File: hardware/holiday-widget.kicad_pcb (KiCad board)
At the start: 4 copper layers, 150 x 75 mm, 119 parts, among them J2 UART, J33 Conn_02x05_Odd_Even, J4 BATTERY POWER, J5 VDC POWER, J7 Speaker, Q1 MMBT3906, Q2 MMBT3906, Q3 MMBT3906, Q4 MMBT3906, Q5 MMBT3906, Q6 MMBT3906, Q7 MMBT3906, Q8 MMBT3906, SW1 SW_Push, SW4 SW_Push, U1 STM32L072RBTx, U2 TPS61200DRC, U3 LIS3DH, U4 IMP23ABSU, U5 TMP102xxDRL, U6 VCNL_4020, U7 PAM8302AAD, U8 OPA355NA

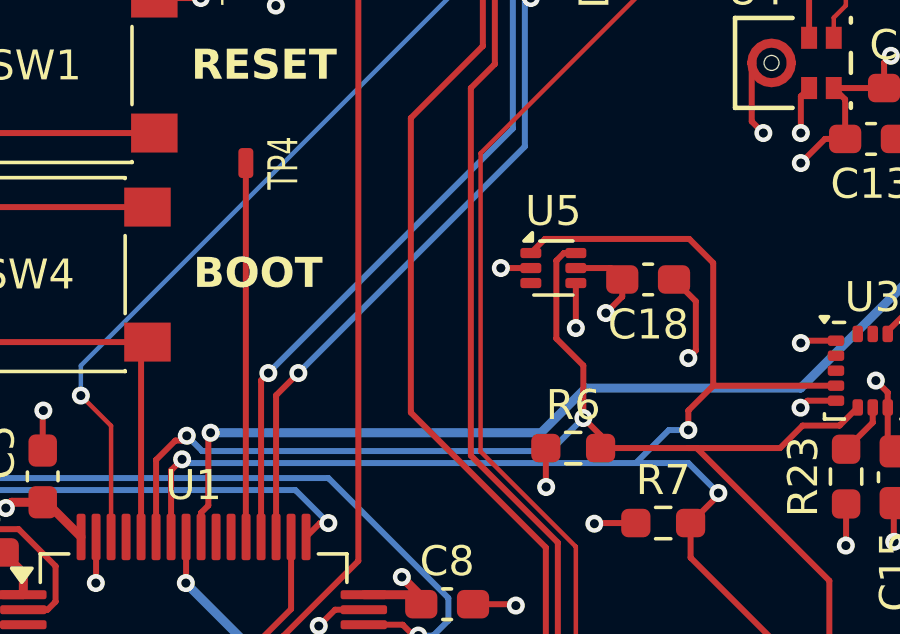
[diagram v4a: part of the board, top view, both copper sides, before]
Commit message: [Hardware] Remove tmp102
No longer using the tmp102 temperature sensor, so remove it from the board.
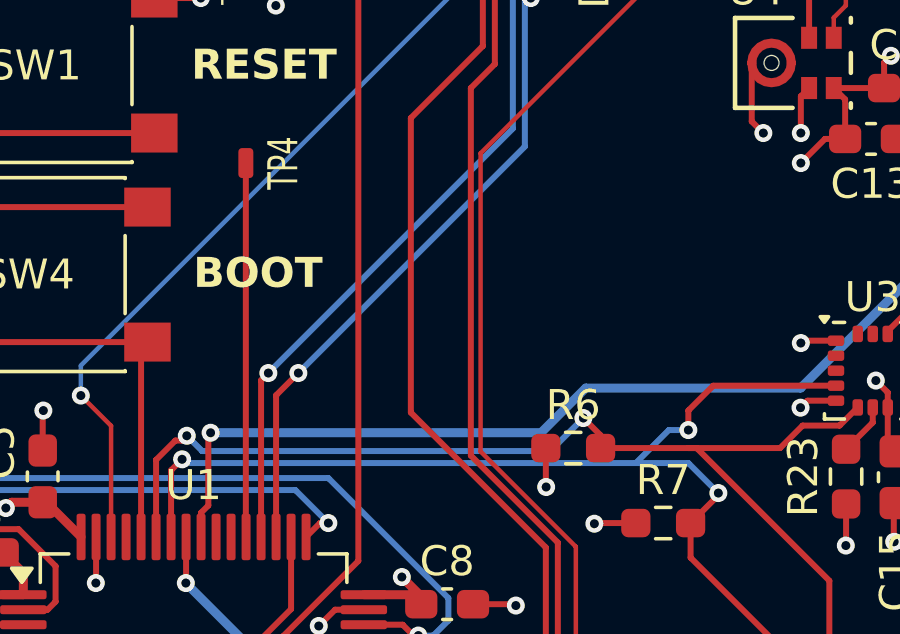
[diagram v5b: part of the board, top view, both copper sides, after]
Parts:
- removed C18: 10n, Capacitor_SMD:C_0603_1608Metric_Pad1.08x0.95mm_HandSolder
- removed U5: TMP102xxDRL, Package_TO_SOT_SMD:SOT-563
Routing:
- net /I2C.SCL: track 111.2 -> 100.5 mm
- net /I2C.SDA: track 103.4 -> 97.0 mm
- net /GND: track 100.0 -> 94.5 mm, vias 63 -> 60
- net /VDD: track 82.2 -> 79.2 mm, vias 32 -> 31

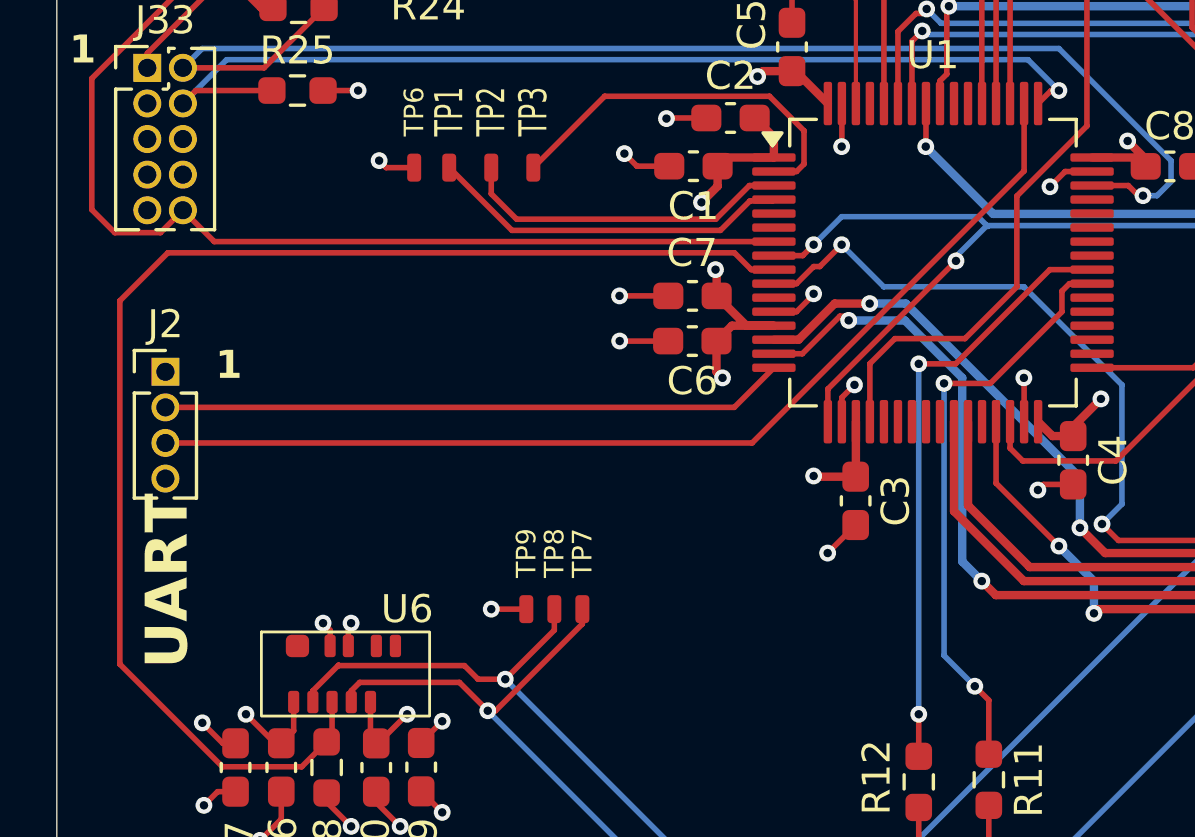
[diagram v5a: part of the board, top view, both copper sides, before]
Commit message: [Hardware] Resize UART header to be 2.54mm pitch.
Previous revision had incorrectly sized pinout, correct this.
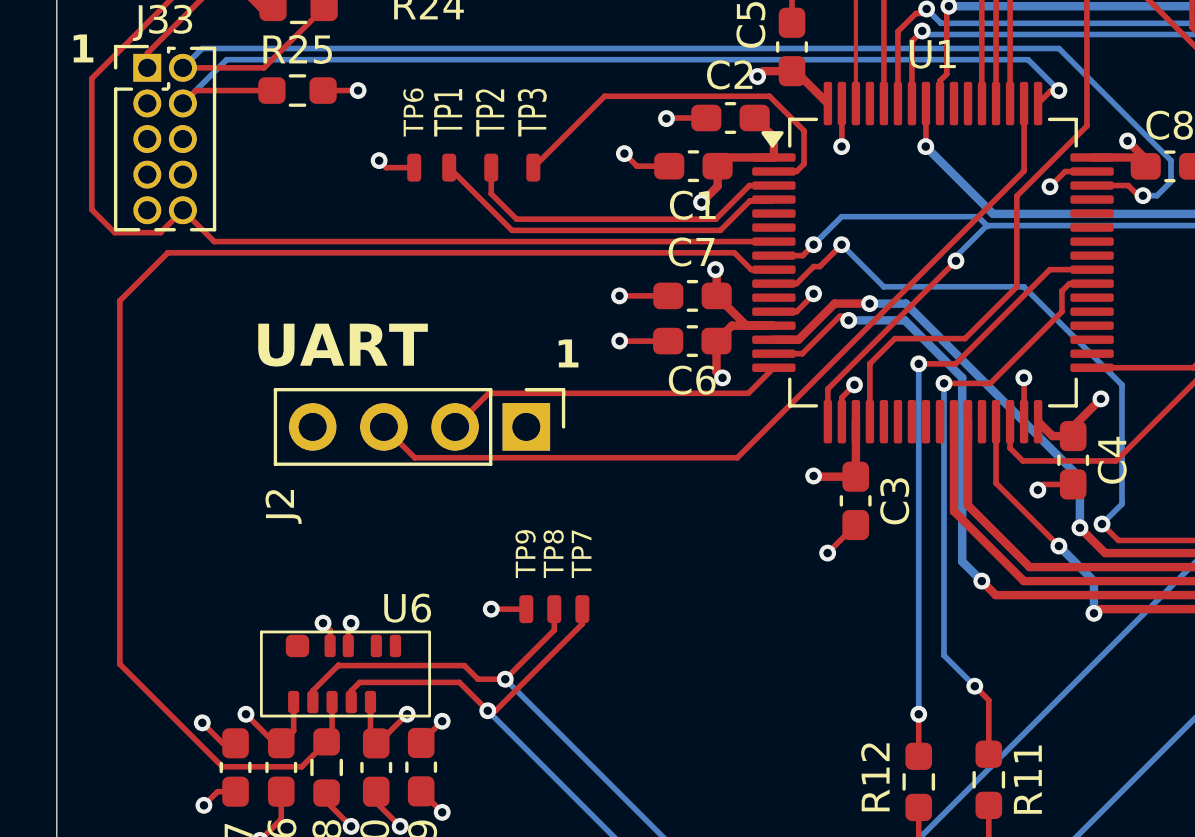
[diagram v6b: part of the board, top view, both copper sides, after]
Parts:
- J2: footprint Connector_PinHeader_1.27mm:PinHeader_1x04_P1.27mm_Vertical -> Connector_PinHeader_2.54mm:PinHeader_1x04_P2.54mm_Vertical
- moved J2 13.0 mm to (130.8, 125.0), turned to -90 degrees
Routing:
- net /UART.TX: track 22.3 -> 12.2 mm
- net /UART.RX: track 37.1 -> 29.9 mm
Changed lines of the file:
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@@
 		)
 	)
-	(footprint "Connector_PinHeader_1.27mm:PinHeader_1x04_P1.27mm_Vertical"
+	(footprint "Connector_PinHeader_2.54mm:PinHeader_1x04_P2.54mm_Vertical"
 		(layer "F.Cu")
-		(at 117.87536 123.032355)
-		(descr "Through hole straight pin header, 1x04, 1.27mm pitch, single row")
-		(tags "Through hole pin header THT 1x04 1.27mm single row")
+		(at 130.75 125 -90)
+		(descr "Through hole straight pin header, 1x04, 2.54mm pitch, single row")
+		(tags "Through hole pin header THT 1x04 2.54mm single row")
 		(property "Reference" "J2"
-			(at 0 -1.695 0)
+			(at 2.75 8.75 90)
 			(layer "F.SilkS")
 			(effects
 				(font
 					(size 1 1)
-					(thickness 0.153)
+					(thickness 0.15)
 				)
 			)
 		)
 		(property "Value" "UART"
-			(at 0 5.505 0)
+			(at 0 9.95 90)
 			(layer "F.Fab")
 			(effects
@@
 			)
 		)
-		(property "Footprint" "Connector_PinHeader_1.27mm:PinHeader_1x04_P1.27mm_Vertical"
-			(at 0 0 0)
+		(property "Footprint" "Connector_PinHeader_2.54mm:PinHeader_1x04_P2.54mm_Vertical"
+			(at 0 0 -90)
 			(unlocked yes)
 			(layer "F.Fab")
@@
 		)
 		(property "Datasheet" ""
-			(at 0 0 0)
+			(at 0 0 -90)
 			(unlocked yes)
 			(layer "F.Fab")
@@
 		)
 		(property "Description" "Generic connector, single row, 01x04, script generated (kicad-library-utils/schlib/autogen/connector/)"
-			(at 0 0 0)
+			(at 0 0 -90)
 			(unlocked yes)
 			(layer "F.Fab")
@@
 		(attr through_hole)
 		(fp_line
-			(start -1.11 -0.76)
-			(end 0 -0.76)
+			(start -1.33 8.95)
+			(end 1.33 8.95)
 			(stroke
 				(width 0.12)
@@
 		)
 		(fp_line
-			(start -1.11 0)
-			(end -1.11 -0.76)
+			(start -1.33 1.27)
+			(end -1.33 8.95)
 			(stroke
 				(width 0.12)
@@
 		)
 		(fp_line
-			(start -1.11 0.76)
-			(end -1.11 4.505)
+			(start -1.33 1.27)
+			(end 1.33 1.27)
 			(stroke
 				(width 0.12)
@@
 		)
 		(fp_line
-			(start -1.11 0.76)
-			(end -0.563471 0.76)
+			(start 1.33 1.27)
+			(end 1.33 8.95)
 			(stroke
 				(width 0.12)
@@
 		)
 		(fp_line
-			(start -1.11 4.505)
-			(end -0.30753 4.505)
+			(start -1.33 0)
+			(end -1.33 -1.33)
 			(stroke
 				(width 0.12)
@@
 		)
 		(fp_line
-			(start 0.30753 4.505)
-			(end 1.11 4.505)
+			(start -1.33 -1.33)
+			(end 0 -1.33)
 			(stroke
 				(width 0.12)
@@
 		)
 		(fp_line
-			(start 0.563471 0.76)
-			(end 1.11 0.76)
-			(stroke
-				(width 0.12)
-				(type solid)
-			)
-			(layer "F.SilkS")
-		)
-		(fp_line
-			(start 1.11 0.76)
-			(end 1.11 4.505)
-			(stroke
-				(width 0.12)
-				(type solid)
-			)
-			(layer "F.SilkS")
-		)
-		(fp_line
-			(start -1.55 -1.15)
-			(end -1.55 4.95)
+			(start -1.8 9.4)
+			(end 1.8 9.4)
 			(stroke
 				(width 0.05)
@@
 		)
 		(fp_line
-			(start -1.55 4.95)
-			(end 1.55 4.95)
+			(start 1.8 9.4)
+			(end 1.8 -1.8)
 			(stroke
 				(width 0.05)
@@
 		)
 		(fp_line
-			(start 1.55 -1.15)
-			(end -1.55 -1.15)
+			(start -1.8 -1.8)
+			(end -1.8 9.4)
 			(stroke
 				(width 0.05)
@@
 		)
 		(fp_line
-			(start 1.55 4.95)
-			(end 1.55 -1.15)
+			(start 1.8 -1.8)
+			(end -1.8 -1.8)
 			(stroke
 				(width 0.05)
@@
 		)
 		(fp_line
-			(start -1.05 -0.11)
-			(end -0.525 -0.635)
+			(start -1.27 8.89)
+			(end -1.27 -0.635)
 			(stroke
 				(width 0.1)
@@
 		)
 		(fp_line
-			(start -1.05 4.445)
-			(end -1.05 -0.11)
+			(start 1.27 8.89)
+			(end -1.27 8.89)
 			(stroke
 				(width 0.1)
@@
 		)
 		(fp_line
-			(start -0.525 -0.635)
-			(end 1.05 -0.635)
+			(start -1.27 -0.635)
+			(end -0.635 -1.27)
 			(stroke
 				(width 0.1)
@@
 		)
 		(fp_line
-			(start 1.05 -0.635)
-			(end 1.05 4.445)
+			(start -0.635 -1.27)
+			(end 1.27 -1.27)
 			(stroke
 				(width 0.1)
@@
 		)
 		(fp_line
-			(start 1.05 4.445)
-			(end -1.05 4.445)
+			(start 1.27 -1.27)
+			(end 1.27 8.89)
 			(stroke
 				(width 0.1)
@@
 		)
 		(fp_text user "${REFERENCE}"
-			(at 0 1.905 90)
+			(at 0 3.81 360)
 			(layer "F.Fab")
 			(effects
@@
 		)
 		(pad "1" thru_hole rect
-			(at 0 0)
-			(size 1 1)
-			(drill 0.65)
+			(at 0 0 270)
+			(size 1.7 1.7)
+			(drill 1)
 			(layers "*.Cu" "*.Mask")
 			(remove_unused_layers no)
@@
 		)
 		(pad "2" thru_hole oval
-			(at 0 1.27)
-			(size 1 1)
-			(drill 0.65)
+			(at 0 2.54 270)
+			(size 1.7 1.7)
+			(drill 1)
 			(layers "*.Cu" "*.Mask")
 			(remove_unused_layers no)
@@
 		)
 		(pad "3" thru_hole oval
-			(at 0 2.54)
-			(size 1 1)
-			(drill 0.65)
+			(at 0 5.08 270)
+			(size 1.7 1.7)
+			(drill 1)
 			(layers "*.Cu" "*.Mask")
 			(remove_unused_layers no)
@@
 		)
 		(pad "4" thru_hole oval
-			(at 0 3.81)
-			(size 1 1)
-			(drill 0.65)
+			(at 0 7.62 270)
+			(size 1.7 1.7)
+			(drill 1)
 			(layers "*.Cu" "*.Mask")
 			(remove_unused_layers no)
@@
 			(pintype "passive")
 		)
-		(model "${KICAD8_3DMODEL_DIR}/Connector_PinHeader_1.27mm.3dshapes/PinHeader_1x04_P1.27mm_Vertical.wrl"
+		(model "${KICAD8_3DMODEL_DIR}/Connector_PinHeader_2.54mm.3dshapes/PinHeader_1x04_P2.54mm_Vertical.wrl"
 			(offset
 				(xyz 0 0 0)
@@
 	)
 	(gr_text "UART"
-		(at 118.818028 133.620197 90)
+		(at 121 123 0)
 		(layer "F.SilkS")
 		(effects
@@
 	)
 	(gr_text "1"
-		(at 119.66126 123.371122 0)
+		(at 131.75 123 0)
 		(layer "F.SilkS")
 		(effects
@@
 	)
 	(segment
-		(start 138.169305 124.302355)
-		(end 139.582934 122.888726)
+		(start 138.67166 123.8)
+		(end 129.41 123.8)
 		(width 0.2)
 		(layer "F.Cu")
@@
 	)
 	(segment
-		(start 117.87536 124.302355)
-		(end 138.169305 124.302355)
+		(start 139.582934 122.888726)
+		(end 138.67166 123.8)
 		(width 0.2)
 		(layer "F.Cu")
@@
 	)
 	(segment
-		(start 148.507934 113.463726)
-		(end 148.507934 115.869884)
+		(start 129.41 123.8)
+		(end 128.21 125)
+		(width 0.2)
+		(layer "F.Cu")
+		(net 12)
+	)
+	(segment
+		(start 148.507934 115.869884)
+		(end 138.277818 126.1)
 		(width 0.2)
 		(layer "F.Cu")
@@
 	)
 	(segment
-		(start 138.805463 125.572355)
-		(end 117.87536 125.572355)
+		(start 126.77 126.1)
+		(end 125.67 125)
 		(width 0.2)
 		(layer "F.Cu")
@@
 	)
 	(segment
-		(start 148.507934 115.869884)
-		(end 138.805463 125.572355)
+		(start 148.507934 113.463726)
+		(end 148.507934 115.869884)
+		(width 0.2)
+		(layer "F.Cu")
+		(net 13)
+	)
+	(segment
+		(start 138.277818 126.1)
+		(end 126.77 126.1)
 		(width 0.2)
 		(layer "F.Cu")
